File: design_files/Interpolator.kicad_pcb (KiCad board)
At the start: 4 copper layers, 78 x 46 mm, 73 parts, among them J1 DA15_Receptacle_MountingHoles, J2 DA15_Receptacle_MountingHoles, J3 Conn_01x12, J4 Conn_01x12, SW1 SW_Push, U1 UA9638C, U2 UA9638C, U3 ICTW8, U5 24AA02-OT, U6 MCP1754S-3302xMB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

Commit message: Add a readme and license
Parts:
- X1: footprint encoder-interpolator:Oscillator_SMD_EuroQuartz_XO91-4Pin_7.0x5.0mm -> encoder-interpolator:Oscillator5x3.2mm
- moved X1 2.35 mm to (158.5, 48.0)
- moved C12 2.00 mm to (162.3, 48.1)
- renumbered R20 to R19, R22 to R20
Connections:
- D1 pad 1: Net-(D1-K) -> FAULT
- D1 pad 2: +3.3V -> Net-(D1-A)
- D2 pad 1: Net-(D2-K) -> STATUS
- D2 pad 2: +3.3V -> Net-(D2-A)
- RN4 pad 2: GND -> Net-(D3-K)
- RN4 pad 3: FAULT -> Net-(D1-A)
- RN4 pad 4: STATUS -> Net-(D2-A)
- RN4 pad 5: Net-(D2-K) -> +3.3V
- RN4 pad 6: Net-(D1-K) -> +3.3V
- RN4 pad 7: Net-(D5-K) -> GND
- RN4 pad 8: Net-(D3-K) -> Net-(D5-K)
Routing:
- net +3.3V: track 96.1 -> 110.7 mm, vias 3 -> 4
- net SETUP: track 106.8 -> 119.4 mm
- net Net-(D1-A): track 0.00 -> 5.79 mm
- net FAULT: track 16.1 -> 20.1 mm
- net GND: track 32.1 -> 35.5 mm
- net Net-(D3-K): track 0.00 -> 3.00 mm
- net STATUS: track 11.3 -> 13.5 mm, vias 1 -> 2
- net Net-(D2-A): track 0.00 -> 2.04 mm
- net Net-(D5-K): track 0.00 -> 2.01 mm
- net Net-(J3-Pin_3): track 45.5 -> 43.7 mm

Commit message: Add a BOM and fab notes
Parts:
- X1: value DSC1001 - 24MHz -> DSC1001BE5-024.0000
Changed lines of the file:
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@@
         (effects (font (size 1 1) (thickness 0.15)))
     )
-    (fp_text value "DSC1001 - 24MHz" (at 0 4.1) (layer "F.Fab") hide
+    (fp_text value "DSC1001BE5-024.0000" (at 0 4.1) (layer "F.Fab") hide
         (effects (font (size 1 1) (thickness 0.15)))
     )

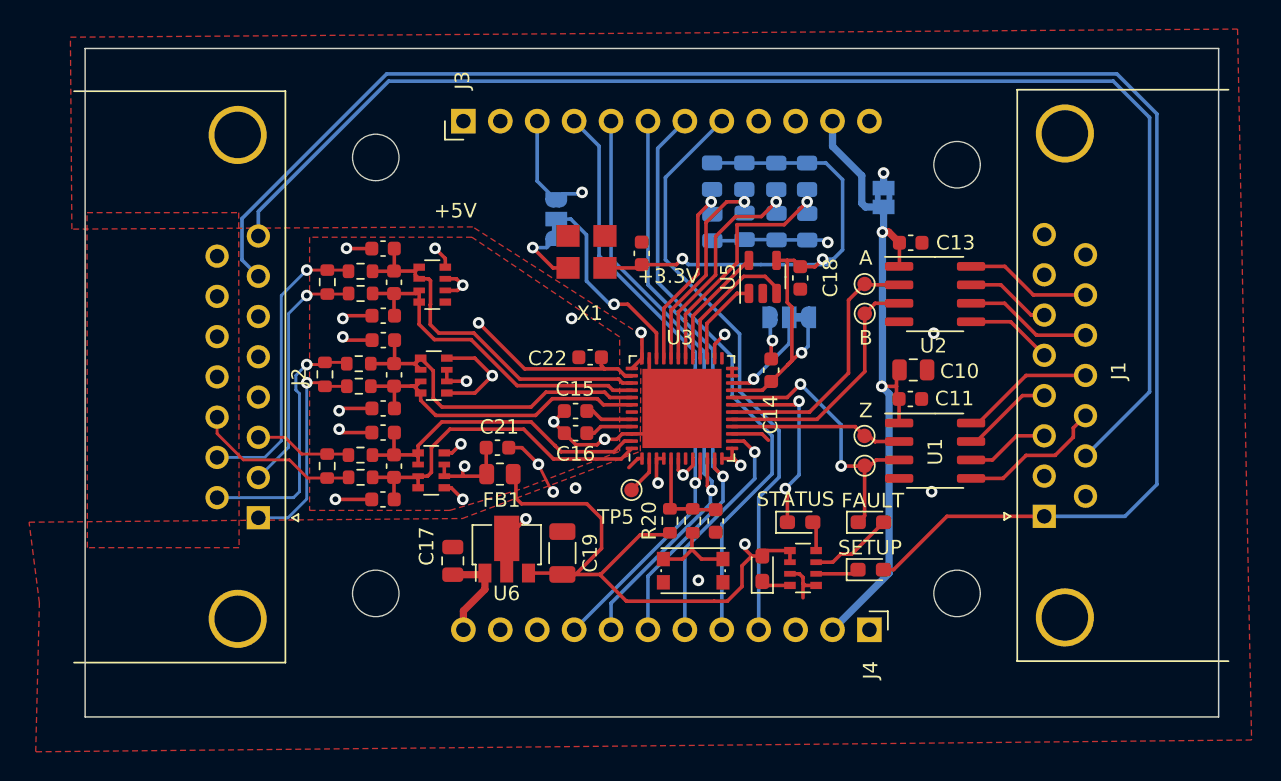
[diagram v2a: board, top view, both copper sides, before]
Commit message: Revision 2, and update kicad version
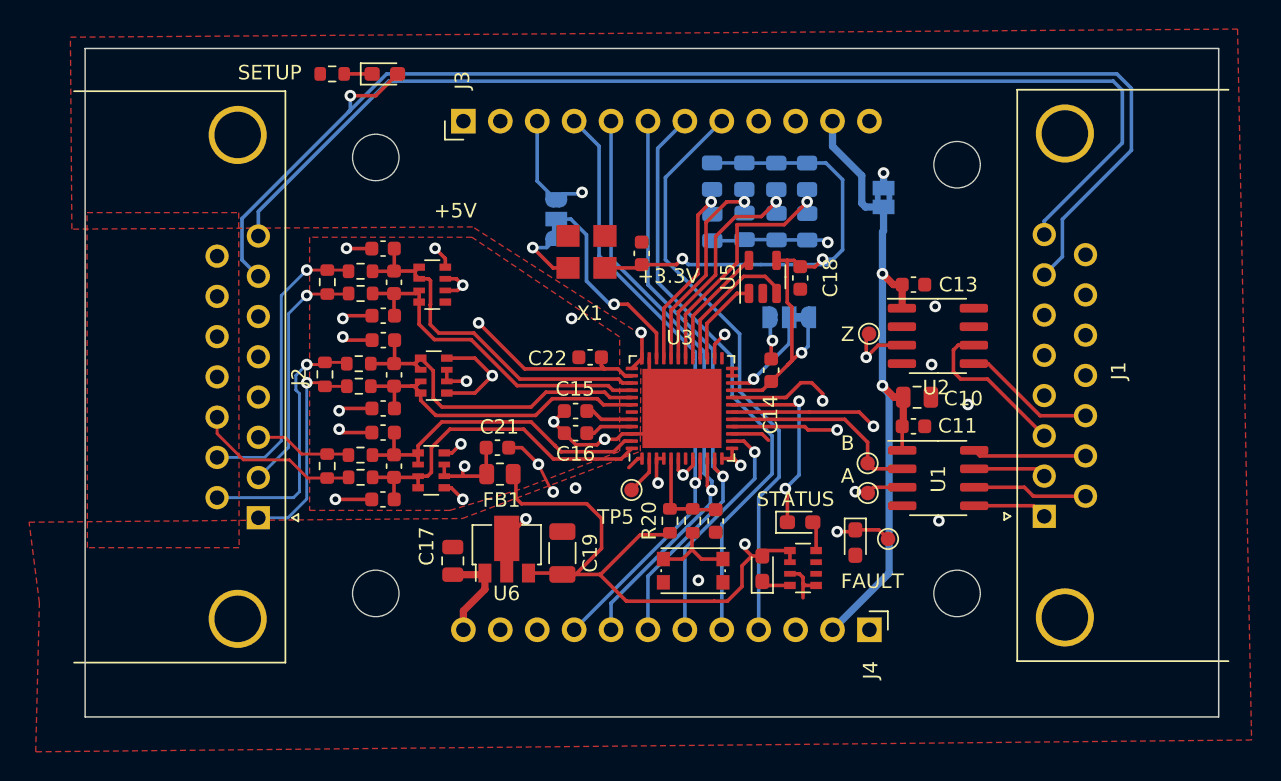
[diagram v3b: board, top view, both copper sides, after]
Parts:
- added R21: 20K, encoder-interpolator:R_0603_1608Metric, F.Cu at (141.0, 35.8)
- moved D3 47.8 mm to (144.6, 35.8)
- moved TP4 15.6 mm to (179.2, 67.8)
- moved TP3 3.43 mm to (177.9, 53.6)
- moved C13 2.89 mm to (181.0, 50.2)
- moved U2 2.89 mm to (182.7, 53.8)
- moved C10 1.90 mm to (181.2, 58.0)
- moved C11 1.89 mm to (181.0, 60.0)
- moved TP1 1.89 mm to (177.8, 62.5)
- moved TP2 1.89 mm to (177.9, 64.6)
- moved U1 1.89 mm to (182.7, 63.6)
- moved D1 1.77 mm to (177.0, 68.0), turned to -90 degrees
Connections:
- J1 pad 1: SETUP -> Net-(U1-2Z)
- J1 pad 10: LIMIT1 -> Net-(J1-P10)
- J1 pad 12: Net-(J1-P12) -> GND
- J1 pad 13: Net-(J1-P13) -> GND
- J1 pad 14: Net-(J1-P14) -> unconnected-(J1-P14-Pad14)
- J1 pad 2: GND -> Net-(U1-1Z)
- J1 pad 3: Net-(U1-2Y) -> Net-(U2-2Y)
- J1 pad 4: Net-(U1-1Z) -> +5V
- J1 pad 5: Net-(U2-2Z) -> +5V
- J1 pad 6: Net-(U2-1Z) -> unconnected-(J1-Pad6)
- J1 pad 7: +5V -> SETUP
- J1 pad 8: +5V -> LIMIT1
- J1 pad 9: GND -> Net-(J1-P9)
- RN4 pad 2: Net-(D3-K) -> unconnected-(RN4-R2.1-Pad2)
- TP1 pad 1: Z -> B
- TP2 pad 1: FAULT -> A
- TP3 pad 1: A -> Z
- TP4 pad 1: B -> FAULT
- U1 pad 2: Z -> B
- U1 pad 3: FAULT -> A
- U1 pad 5: Net-(J1-P111) -> Net-(U1-2Z)
- U1 pad 6: Net-(U1-2Y) -> Net-(J1-P9)
- U1 pad 8: Net-(J1-P12) -> Net-(J1-P10)
- U2 pad 2: A -> unconnected-(U2-1A-Pad2)
- U2 pad 3: B -> Z
- U2 pad 5: Net-(U2-2Z) -> Net-(J1-P111)
- U2 pad 6: Net-(J1-P13) -> Net-(U2-2Y)
- U2 pad 7: Net-(U2-1Z) -> unconnected-(U2-1Z-Pad7)
- U2 pad 8: Net-(J1-P14) -> unconnected-(U2-1Y-Pad8)
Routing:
- net SETUP: track 119.4 -> 90.5 mm, vias 0 -> 1
- net LIMIT1: track 92.9 -> 77.3 mm
- net Net-(U2-2Y): track 0.00 -> 11.1 mm
- net Net-(J1-P12): track 9.23 -> 0.00 mm
- net Net-(J1-P13): track 8.78 -> 0.00 mm
- net Net-(J1-P14): track 8.69 -> 0.00 mm
- net +5V: track 119.9 -> 128.2 mm
- net Net-(J1-P9): track 0.00 -> 7.91 mm
- net Net-(J1-P10): track 0.00 -> 7.82 mm
- net Z: track 11.9 -> 17.9 mm, vias 0 -> 2
- net Net-(U2-2Z): track 5.99 -> 0.00 mm
- net Net-(U2-1Z): track 5.90 -> 0.00 mm
- net Net-(D1-A): track 5.79 -> 0.00 mm
- net Net-(U1-2Y): track 5.72 -> 0.00 mm
- net Net-(U1-2Z): track 0.00 -> 5.32 mm
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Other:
- board text added: "mds - rev 2 - 4/20/25"
- board text removed: "mds - rev 1 - 1/18/25"

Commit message: Pulldown the unused line driver input
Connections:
- U2 pad 2: unconnected-(U2-1A-Pad2) -> GND
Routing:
- net GND: track 34.7 -> 36.5 mm
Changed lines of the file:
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@@
 	(net 66 "unconnected-(RN4-R2.1-Pad2)")
 	(net 67 "Net-(U2-2Y)")
-	(net 68 "unconnected-(U2-1A-Pad2)")
-	(net 69 "unconnected-(U2-1Y-Pad8)")
-	(net 70 "unconnected-(U2-1Z-Pad7)")
+	(net 68 "unconnected-(U2-1Y-Pad8)")
+	(net 69 "unconnected-(U2-1Z-Pad7)")
 	(footprint "encoder-interpolator:R_0603_1608Metric"
 		(layer "F.Cu")
@@
 			(layers "F.Cu" "F.Mask" "F.Paste")
 			(roundrect_rratio 0.25)
-			(net 68 "unconnected-(U2-1A-Pad2)")
+			(net 7 "GND")
 			(pinfunction "1A")
-			(pintype "input+no_connect")
+			(pintype "input")
 		)
 		(pad "3" smd roundrect
@@
 			(layers "F.Cu" "F.Mask" "F.Paste")
 			(roundrect_rratio 0.25)
-			(net 70 "unconnected-(U2-1Z-Pad7)")
+			(net 69 "unconnected-(U2-1Z-Pad7)")
 			(pinfunction "1Z")
 			(pintype "input+no_connect")
@@
 			(layers "F.Cu" "F.Mask" "F.Paste")
 			(roundrect_rratio 0.25)
-			(net 69 "unconnected-(U2-1Y-Pad8)")
+			(net 68 "unconnected-(U2-1Y-Pad8)")
 			(pinfunction "1Y")
 			(pintype "input+no_connect")
@@
 	)
 	(segment
+		(start 179.56 52.5)
+		(end 178.75 52.5)
+		(width 0.25)
+		(layer "F.Cu")
+		(net 7)
+	)
+	(segment
 		(start 171.21 55.365)
 		(end 171.21 54.1896)
@@
 		(width 0.25)
 		(layer "F.Cu")
+		(net 7)
+	)
+	(segment
+		(start 180.205 53.145)
+		(end 179.56 52.5)
+		(width 0.25)
+		(layer "F.Cu")
